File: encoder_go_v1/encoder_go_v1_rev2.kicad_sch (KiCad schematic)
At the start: 7 parts, among them J1 BM05B-SRSS-TB_LF__SN_, J2 optional features, U1 MT6701-SOP8

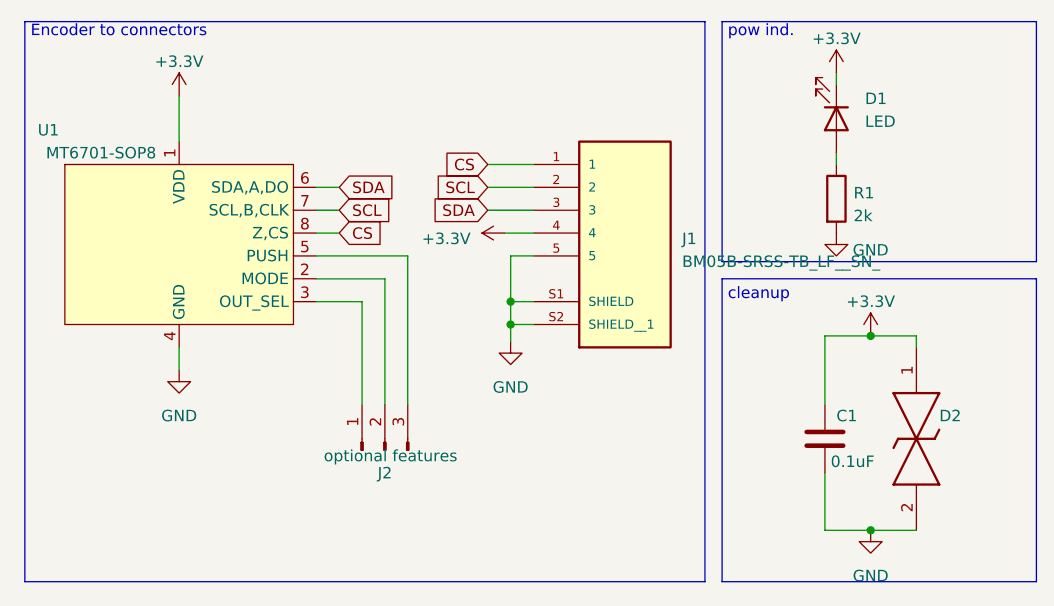
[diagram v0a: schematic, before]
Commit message: remove unused files and edited pcb for cnc mill process
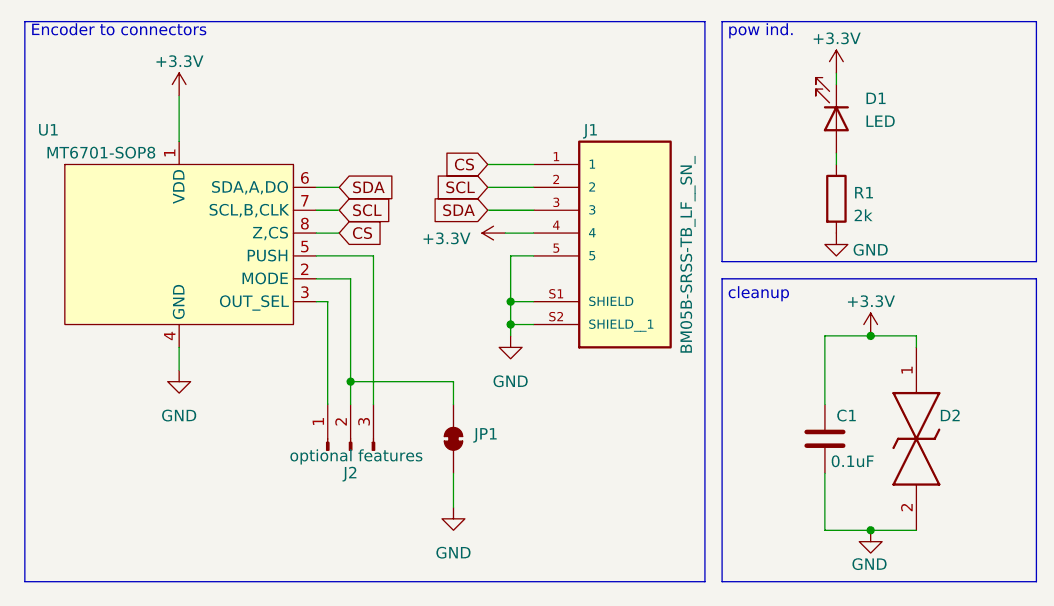
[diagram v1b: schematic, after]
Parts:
- added JP1: SolderJumper_2_Bridged, Jumper:SolderJumper-2_P1.3mm_Bridged_RoundedPad1.0x1.5mm, symbol Jumper:SolderJumper_2_Bridged
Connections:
- net GND: now also JP1.1 (A)
- net at J2.2 (Pin_2), U1.2 (MODE): now also JP1.2 (B)
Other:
- moved on the sheet: J2
